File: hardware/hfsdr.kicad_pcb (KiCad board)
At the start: 2 copper layers, 50 x 25 mm, 8 parts, among them J1 USB_C_Receptacle_USB2.0_16P, U1 SN74CBT3253, U2 XLV320ADC6120IRTER, U3 CH32V30xFxPx, U4 XC6206PxxxMR, Y1 Si5351A-B-GT

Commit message: Update schematic
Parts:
- added C1: 1uF, Capacitor_SMD:C_0805_2012Metric_Pad1.18x1.45mm_HandSolder, F.Cu at (128.2, 63.2)
- added C10: 1uF, Capacitor_SMD:C_0805_2012Metric_Pad1.18x1.45mm_HandSolder, F.Cu at (162.2, 81.2)
- added C11: 100nF, Capacitor_SMD:C_0805_2012Metric_Pad1.18x1.45mm_HandSolder, F.Cu at (162.2, 84.2)
- added C12: 100nF, Capacitor_SMD:C_0805_2012Metric_Pad1.18x1.45mm_HandSolder, F.Cu at (162.2, 87.2)
- added C13: 1uF, Capacitor_SMD:C_0805_2012Metric_Pad1.18x1.45mm_HandSolder, F.Cu at (162.2, 90.2)
- added C14: 1uF, Capacitor_SMD:C_0805_2012Metric_Pad1.18x1.45mm_HandSolder, F.Cu at (167.0, 75.2)
- added C15: 1uF, Capacitor_SMD:C_0805_2012Metric_Pad1.18x1.45mm_HandSolder, F.Cu at (167.0, 78.2)
- added C16: 1uF, Capacitor_SMD:C_0805_2012Metric_Pad1.18x1.45mm_HandSolder, F.Cu at (167.0, 81.2)
- added C17: 100nF, Capacitor_SMD:C_0603_1608Metric_Pad1.08x0.95mm_HandSolder, F.Cu at (110.5, 68.2)
- added C18: 100nF, Capacitor_SMD:C_0603_1608Metric_Pad1.08x0.95mm_HandSolder, F.Cu at (110.5, 70.7)
- added C19: 100nF, Capacitor_SMD:C_0805_2012Metric_Pad1.18x1.45mm_HandSolder, F.Cu at (159.1, 42.2)
- added C2: 100nF, Capacitor_SMD:C_0603_1608Metric_Pad1.08x0.95mm_HandSolder, F.Cu at (130.8, 53.8)
- added C20: 100nF, Capacitor_SMD:C_0805_2012Metric_Pad1.18x1.45mm_HandSolder, F.Cu at (159.1, 45.2)
- added C3: 1nF, Capacitor_SMD:C_0805_2012Metric_Pad1.18x1.45mm_HandSolder, F.Cu at (128.2, 55.8)
- added C4: 100nF, Capacitor_SMD:C_0805_2012Metric_Pad1.18x1.45mm_HandSolder, F.Cu at (157.4, 81.2)
- added C5: 100nF, Capacitor_SMD:C_0805_2012Metric_Pad1.18x1.45mm_HandSolder, F.Cu at (157.4, 84.2)
- added C6: 100nF, Capacitor_SMD:C_0805_2012Metric_Pad1.18x1.45mm_HandSolder, F.Cu at (157.4, 87.2)
- added C7: 100nF, Capacitor_SMD:C_0805_2012Metric_Pad1.18x1.45mm_HandSolder, F.Cu at (157.4, 90.2)
- added C8: 100nF, Capacitor_SMD:C_0805_2012Metric_Pad1.18x1.45mm_HandSolder, F.Cu at (162.2, 75.2)
- added C9: 1uF, Capacitor_SMD:C_0805_2012Metric_Pad1.18x1.45mm_HandSolder, F.Cu at (162.2, 78.2)
- added FB1: GZ2012D601TF, Inductor_SMD:L_0201_0603Metric_Pad0.64x0.40mm_HandSolder, F.Cu at (114.7, 81.5)
- added FB2: GZ2012D601TF, Inductor_SMD:L_0201_0603Metric_Pad0.64x0.40mm_HandSolder, F.Cu at (100.6, 79.0)
- added R3: 10k, Resistor_SMD:R_0603_1608Metric_Pad0.98x0.95mm_HandSolder, F.Cu at (118.5, 50.5)
- added R4: 10k, Resistor_SMD:R_0603_1608Metric_Pad0.98x0.95mm_HandSolder, F.Cu at (112.2, 49.4)
- added SW1: RST, Button_Switch_SMD:SW_Push_1P1T_XKB_TS-1187A, F.Cu at (112.2, 44.1)
- added SW2: BOOT0, Button_Switch_SMD:SW_Push_1P1T_XKB_TS-1187A, F.Cu at (121.0, 44.4)
- added U5: MD57E33QA3, Package_TO_SOT_SMD:SOT-23, F.Cu at (127.8, 84.2)
- U3: value CH32V30xFxPx -> CH32V30xRxTx; footprint Package_SO:TSSOP-20_4.4x6.5mm_P0.65mm -> Package_QFP:LQFP-64_10x10mm_P0.5mm
- U4: value XC6206PxxxMR -> MD57E33QA3; footprint Package_TO_SOT_SMD:SOT-23-3 -> Package_TO_SOT_SMD:SOT-23
- moved U1 27.0 mm to (122.4, 76.2), turned to 0 degrees
- moved Y1 24.3 mm to (102.9, 75.9), turned to 0 degrees
- moved U2 15.8 mm to (109.6, 76.0), turned to 0 degrees
- moved U4 14.3 mm to (126.2, 52.8), turned to 180 degrees
- moved U3 11.2 mm to (110.3, 60.5), turned to -90 degrees
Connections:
- J1 pad A4: Net-(J1-VBUS-PadA4) -> +5V
- J1 pad A6: Net-(U3-PB7) -> DP
- J1 pad A7: Net-(U3-PB6) -> DM
- J1 pad A9: Net-(J1-VBUS-PadA4) -> +5V
- J1 pad B4: Net-(J1-VBUS-PadA4) -> +5V
- J1 pad B6: Net-(U3-PB7) -> DP
- J1 pad B7: Net-(U3-PB6) -> DM
- J1 pad B9: Net-(J1-VBUS-PadA4) -> +5V
- R1 pad 1: GND -> Net-(J1-CC2)
- R1 pad 2: Net-(J1-CC2) -> GND
- U3 pad 1: unconnected-(U3-~{RST}-Pad1) -> +3.3V
- U3 pad 12: unconnected-(U3-PA8/PC9-Pad12) -> GND
- U3 pad 13: unconnected-(U3-SWDIO-Pad13) -> Net-(U3-VDDA)
- U3 pad 16: Net-(U3-PB6) -> unconnected-(U3-PA2-Pad16)
- U3 pad 17: Net-(U3-PB7) -> unconnected-(U3-PA3-Pad17)
- U3 pad 19: MCU_XI -> +3.3V
- U3 pad 3: SCL -> unconnected-(U3-PC14-Pad3)
- U3 pad 4: SDA -> unconnected-(U3-PC15-Pad4)
- U3 pad 5: WS -> Net-(U3-OSC_IN)
- U3 pad 6: CK -> unconnected-(U3-OSC_OUT-Pad6)
- U3 pad 7: unconnected-(U3-PB14-Pad7) -> Net-(U3-~{RST})
- U3 pad 8: SD -> unconnected-(U3-PC0-Pad8)
- U3 pad 9: MCK -> unconnected-(U3-PC1-Pad9)
- U4 pad 2: unconnected-(U4-VO-Pad2) -> +5V
- U4 pad 3: unconnected-(U4-VI-Pad3) -> +3.3V
- Y1 pad 1: unconnected-(Y1-VDD-Pad1) -> Net-(Y1-VDD)
- Y1 pad 7: unconnected-(Y1-VDDO-Pad7) -> Net-(Y1-VDDO)
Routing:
- net DP: track 0.00 -> 18.5 mm
- net DM: track 0.00 -> 18.3 mm
- net MCU_XI: track 13.4 -> 0.00 mm
- net +5V: track 0.00 -> 12.2 mm
- net unconnected-(U1-2A-Pad9): track 10.5 -> 0.00 mm
- net Net-(U3-PB7): track 9.99 -> 0.00 mm
- net Net-(U3-PB6): track 9.72 -> 0.00 mm
- net Net-(U1-S0): track 9.67 -> 0.00 mm
- net Net-(U1-2B3): track 9.24 -> 0.00 mm, vias 2 -> 0
- net Net-(U1-S1): track 9.07 -> 0.00 mm
- net MCK: track 8.92 -> 0.00 mm, vias 2 -> 0
- net Net-(U1-2B1): track 8.76 -> 0.00 mm, vias 2 -> 0
- net Net-(U1-2B2): track 8.71 -> 0.00 mm
- net SCL: track 7.48 -> 0.00 mm
- net SD: track 7.16 -> 0.00 mm
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
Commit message: amp and audio
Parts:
- added C21: 100nF, Capacitor_SMD:C_0805_2012Metric_Pad1.18x1.45mm_HandSolder, F.Cu at (149.5, 57.1)
- added C22: 100nF, Capacitor_SMD:C_0805_2012Metric_Pad1.18x1.45mm_HandSolder, F.Cu at (149.5, 60.1)
- added C23: 100nF, Capacitor_SMD:C_0805_2012Metric_Pad1.18x1.45mm_HandSolder, F.Cu at (146.2, 72.8)
- added FB3: GZ2012D601TF, Inductor_SMD:L_0805_2012Metric_Pad1.05x1.20mm_HandSolder, F.Cu at (149.6, 54.2)
- added U6: BGA2817, Package_TO_SOT_SMD:SOT-363_SC-70-6, F.Cu at (154.1, 57.6)
- added U7: TP4054, Package_TO_SOT_SMD:TSOT-23-5, F.Cu at (146.4, 69.0)
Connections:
- C1 pad 1: +5V -> VBUS
- C2 pad 1: +5V -> VBUS
- C3 pad 1: +5V -> VBUS
- J1 pad A4: +5V -> VBUS
- J1 pad A9: +5V -> VBUS
- J1 pad B4: +5V -> VBUS
- J1 pad B9: +5V -> VBUS
- U1 pad 9: unconnected-(U1-2A-Pad9) -> Net-(U1-2A)
- U3 pad 20: unconnected-(U3-PA4-Pad20) -> DAC1_OUT
- U3 pad 21: unconnected-(U3-PA5-Pad21) -> DAC2_OUT
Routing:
- net +5V: track 12.2 -> 9.52 mm
- net VBUS: track 0.00 -> 2.68 mm

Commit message: arrange pcb
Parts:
- added C24: 100nF, Capacitor_SMD:C_0805_2012Metric_Pad1.18x1.45mm_HandSolder, F.Cu at (102.5, 49.5)
- added C25: 1uF, Capacitor_SMD:C_0805_2012Metric_Pad1.18x1.45mm_HandSolder, F.Cu at (109.0, 49.5)
- added C26: 100nF, Capacitor_SMD:C_0805_2012Metric_Pad1.18x1.45mm_HandSolder, F.Cu at (101.0, 51.0)
- added C27: 1uF, Capacitor_SMD:C_0805_2012Metric_Pad1.18x1.45mm_HandSolder, F.Cu at (159.8, 69.8)
- added FB4: GZ2012D601TF, Inductor_SMD:L_0805_2012Metric_Pad1.05x1.20mm_HandSolder, F.Cu at (164.7, 60.6)
- added FB5: GZ2012D601TF, Inductor_SMD:L_0805_2012Metric_Pad1.05x1.20mm_HandSolder, F.Cu at (164.7, 63.4)
- added FB6: GZ2012D601TF, Inductor_SMD:L_0805_2012Metric_Pad1.05x1.20mm_HandSolder, F.Cu at (164.7, 66.1)
- added FB7: GZ2012D601TF, Inductor_SMD:L_0805_2012Metric_Pad1.05x1.20mm_HandSolder, F.Cu at (164.7, 68.9)
- added R5: 10k, Resistor_SMD:R_0603_1608Metric_Pad0.98x0.95mm_HandSolder, F.Cu at (99.0, 47.5)
- added R6: 10k, Resistor_SMD:R_0603_1608Metric_Pad0.98x0.95mm_HandSolder, F.Cu at (100.8, 46.0)
- added U8: NS4263_C2829094, easyeda:SOIC-16_L9.9-W3.9-P1.27-LS6.0-BL, F.Cu at (99.5, 38.6)
- FB1, FB2: footprint Inductor_SMD:L_0201_0603Metric_Pad0.64x0.40mm_HandSolder -> Inductor_SMD:L_0805_2012Metric_Pad1.05x1.20mm_HandSolder
- moved U5 48.5 mm to (93.8, 49.8), turned to -90 degrees
- moved U1 36.4 mm to (88.5, 63.0)
- moved C17 34.6 mm to (141.9, 82.8)
- moved FB1 28.3 mm to (115.9, 53.2), turned to 180 degrees
- moved FB2 27.6 mm to (92.2, 52.8), turned to -90 degrees
- moved C18 26.7 mm to (134.4, 82.8)
- moved Y1 21.4 mm to (95.0, 56.0), turned to 90 degrees
- moved U2 19.5 mm to (95.8, 62.2), turned to 90 degrees
- moved SW1 11.4 mm to (123.5, 42.5)
- moved SW2 11.4 mm to (132.2, 42.8)
- moved U3 2.37 mm to (108.1, 59.6), turned to -135 degrees
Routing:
- net DP: track 18.5 -> 3.75 mm
- net DM: track 18.3 -> 4.76 mm
- net SCL: track 0.00 -> 11.2 mm
- net MCK: track 0.00 -> 10.2 mm
- net SDA: track 0.00 -> 9.74 mm
- net +3.3V: track 0.00 -> 5.90 mm
- net SD: track 0.00 -> 5.70 mm
- net CK: track 0.00 -> 5.07 mm
- net WS: track 0.00 -> 4.66 mm
- net Net-(U3-VDDA): track 0.00 -> 4.49 mm

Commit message: battery switching
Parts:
- added C28: 1uF, Capacitor_SMD:C_0805_2012Metric_Pad1.18x1.45mm_HandSolder, F.Cu at (123.2, 50.5)
- added D1: 1N5819WS, Diode_SMD:D_SOD-323, F.Cu at (127.0, 53.5)
- added Q1: AO3401A, Package_TO_SOT_SMD:SOT-23, F.Cu at (123.5, 53.4)
- added R7: 100k, Resistor_SMD:R_0805_2012Metric_Pad1.20x1.40mm_HandSolder, F.Cu at (124.0, 56.5)
- added R8: 2k, Resistor_SMD:R_0805_2012Metric_Pad1.20x1.40mm_HandSolder, F.Cu at (150.8, 70.3)
- added R9: 2k, Resistor_SMD:R_0805_2012Metric_Pad1.20x1.40mm_HandSolder, F.Cu at (150.8, 73.2)
- C17, C18, C2: footprint Capacitor_SMD:C_0603_1608Metric_Pad1.08x0.95mm_HandSolder -> Capacitor_SMD:C_0805_2012Metric_Pad1.18x1.45mm_HandSolder
- R1, R2, R3, R4, R5, R6: footprint Resistor_SMD:R_0603_1608Metric_Pad0.98x0.95mm_HandSolder -> Resistor_SMD:R_0805_2012Metric_Pad1.20x1.40mm_HandSolder
- U1: footprint Package_SO:TSSOP-16_4.4x5mm_P0.65mm -> Package_SO:SOIC-16_3.9x9.9mm_P1.27mm
- moved C13 55.0 mm to (120.5, 54.3), turned to -90 degrees
- moved U7 29.8 mm to (126.4, 47.0)
- moved U6 16.3 mm to (146.2, 43.2)
- moved U4 7.35 mm to (119.2, 50.5)
- moved R3 2.26 mm to (116.2, 50.2)
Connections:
- U7 pad 1: unconnected-(U7-~{CHRG}-Pad1) -> Net-(D2-K)
- U7 pad 5: unconnected-(U7-PROG-Pad5) -> Net-(U7-PROG)
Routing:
- net VBUS: track 2.68 -> 12.7 mm
- net GND: track 8.65 -> 6.61 mm
- net +5V: track 9.52 -> 7.84 mm

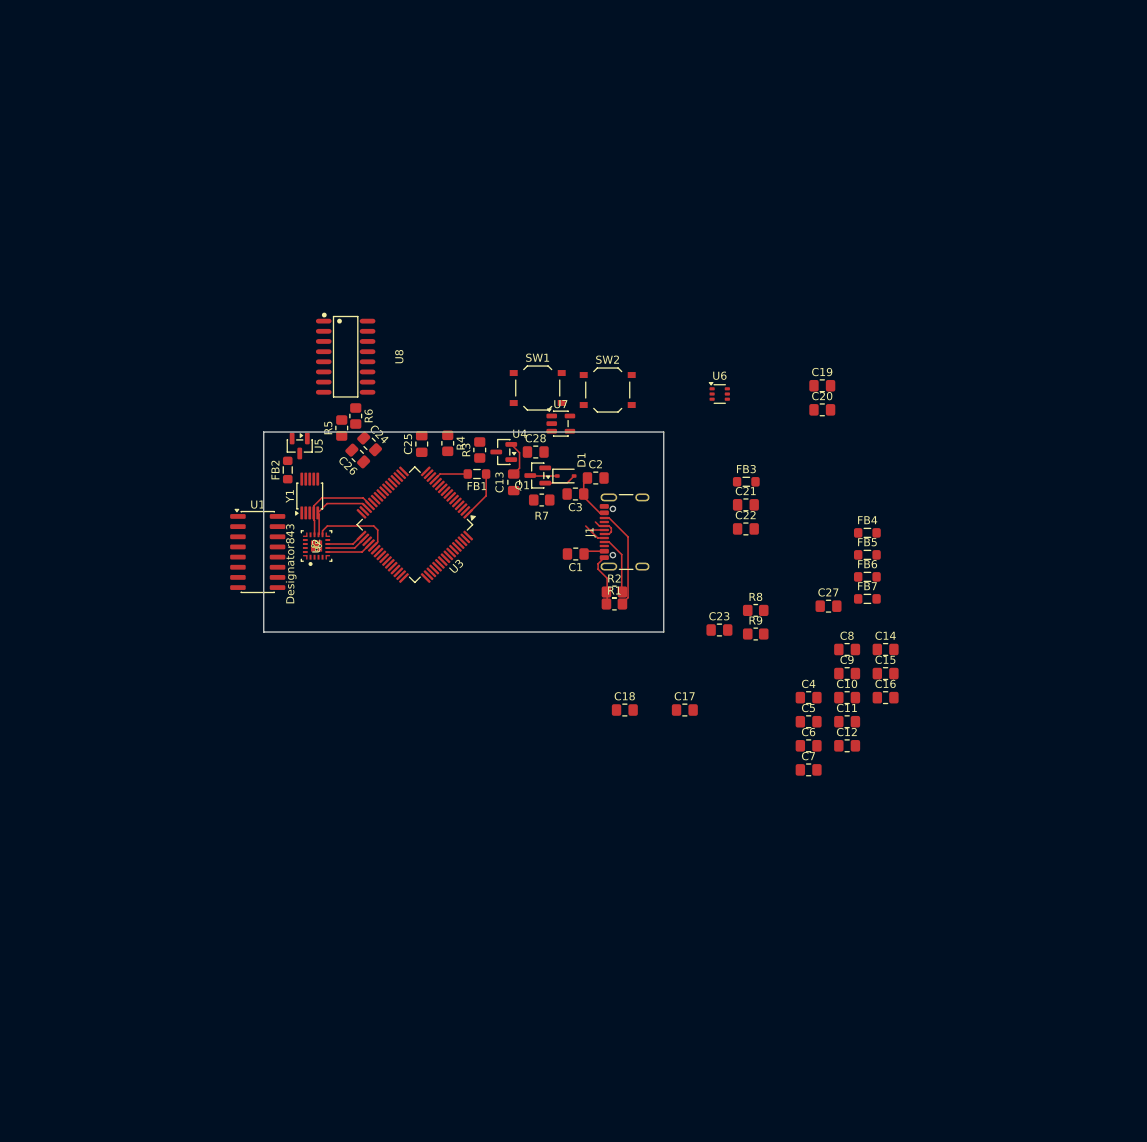
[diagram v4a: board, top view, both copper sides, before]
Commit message: initial component layout
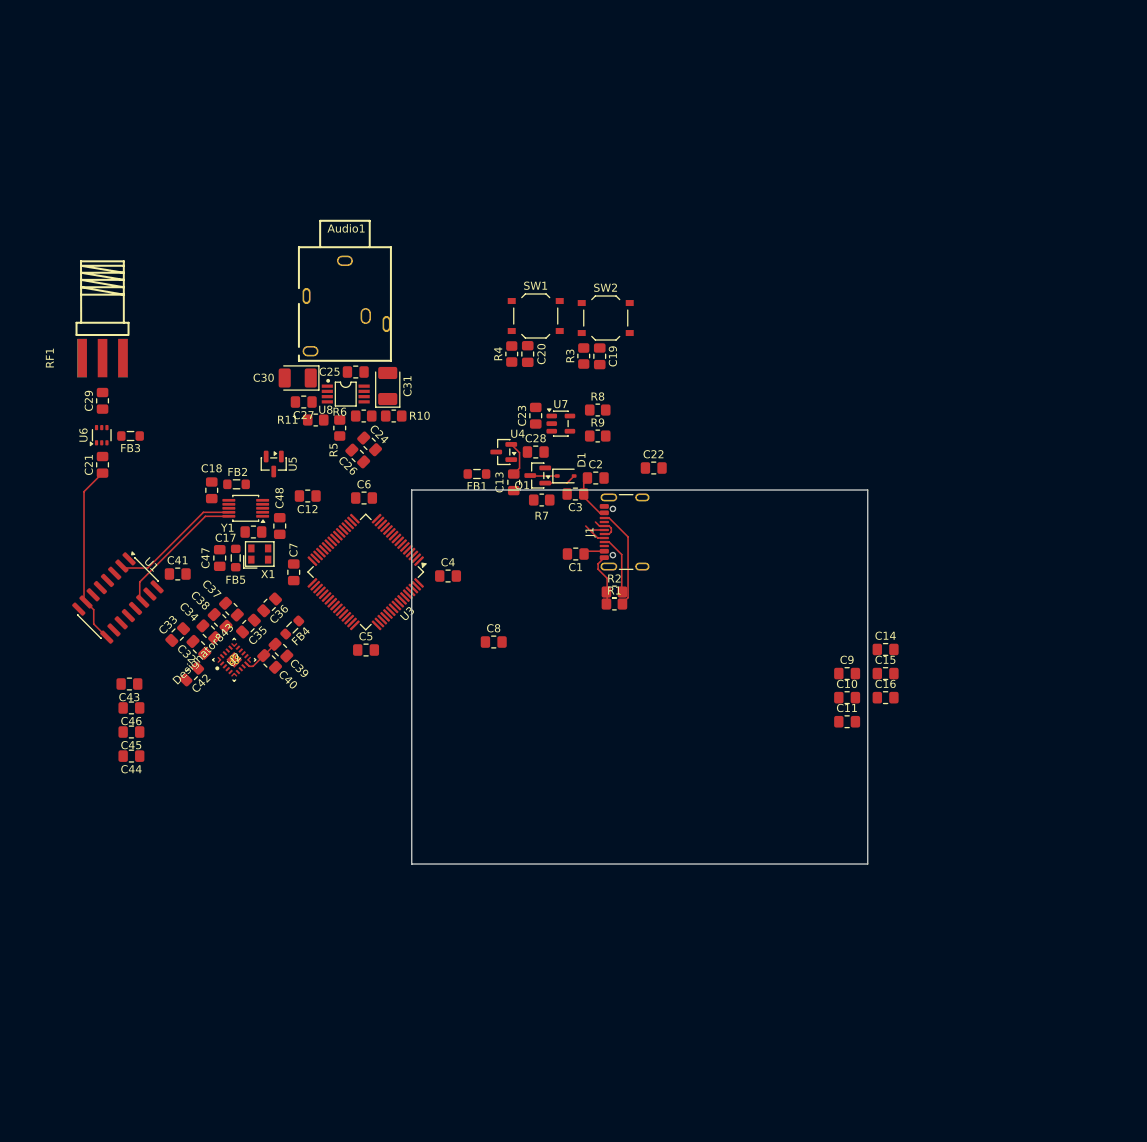
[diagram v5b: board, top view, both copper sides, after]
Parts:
- removed FB6, FB7: GZ2012D601TF, Inductor_SMD:L_0805_2012Metric_Pad1.05x1.20mm_HandSolder
- added Audio1: PJ-3240-5A, easyeda:AUDIO-TH_PJ-3240-5A, F.Cu at (99.6, 32.2)
- added C29: 1uF, Capacitor_SMD:C_0805_2012Metric_Pad1.18x1.45mm_HandSolder, F.Cu at (69.1, 44.1)
- added C30: 100uF, Capacitor_Tantalum_SMD:CP_EIA-3528-15_AVX-H_HandSolder, F.Cu at (93.5, 41.2)
- added C31: 100uF, Capacitor_Tantalum_SMD:CP_EIA-3528-15_AVX-H_HandSolder, F.Cu at (104.8, 42.2)
- added C32: 1uF, Capacitor_SMD:C_0805_2012Metric_Pad1.18x1.45mm_HandSolder, F.Cu at (81.1, 74.9)
- added C33: 10uF, Capacitor_SMD:C_0805_2012Metric_Pad1.18x1.45mm_HandSolder, F.Cu at (78.5, 73.3)
- added C34: 100nF, Capacitor_SMD:C_0805_2012Metric_Pad1.18x1.45mm_HandSolder, F.Cu at (82.4, 73.0)
- added C35: 100nF, Capacitor_SMD:C_0805_2012Metric_Pad1.18x1.45mm_HandSolder, F.Cu at (87.3, 72.3)
- added C36: 10uF, Capacitor_SMD:C_0805_2012Metric_Pad1.18x1.45mm_HandSolder, F.Cu at (90.0, 69.6)
- added C37: 100nF, Capacitor_SMD:C_0805_2012Metric_Pad1.18x1.45mm_HandSolder, F.Cu at (85.2, 70.1)
- added C38: 1uF, Capacitor_SMD:C_0805_2012Metric_Pad1.18x1.45mm_HandSolder, F.Cu at (83.8, 71.6)
- added C39: 100nF, Capacitor_SMD:C_0805_2012Metric_Pad1.18x1.45mm_HandSolder, F.Cu at (91.4, 75.3)
- added C40: 10uF, Capacitor_SMD:C_0805_2012Metric_Pad1.18x1.45mm_HandSolder, F.Cu at (90.0, 76.7)
- added C41: 100nF, Capacitor_SMD:C_0805_2012Metric_Pad1.18x1.45mm_HandSolder, F.Cu at (78.5, 65.8)
- added C42: 1uF, Capacitor_SMD:C_0805_2012Metric_Pad1.18x1.45mm_HandSolder, F.Cu at (80.2, 78.2)
- added C43: 2.2nF, Capacitor_SMD:C_0805_2012Metric_Pad1.18x1.45mm_HandSolder, F.Cu at (72.5, 79.5)
- added C44: 2.2nF, Capacitor_SMD:C_0805_2012Metric_Pad1.18x1.45mm_HandSolder, F.Cu at (72.7, 88.5)
- added C45: 2.2nF, Capacitor_SMD:C_0805_2012Metric_Pad1.18x1.45mm_HandSolder, F.Cu at (72.7, 85.5)
- added C46: 2.2nF, Capacitor_SMD:C_0805_2012Metric_Pad1.18x1.45mm_HandSolder, F.Cu at (72.7, 82.5)
- added C47: 100nF, Capacitor_SMD:C_0805_2012Metric_Pad1.18x1.45mm_HandSolder, F.Cu at (83.8, 63.8)
- added C48: 100nF, Capacitor_SMD:C_0805_2012Metric_Pad1.18x1.45mm_HandSolder, F.Cu at (91.2, 59.8)
- added R10: 20k, Resistor_SMD:R_0805_2012Metric_Pad1.20x1.40mm_HandSolder, F.Cu at (105.5, 46.0)
- added R11: 20k, Resistor_SMD:R_0805_2012Metric_Pad1.20x1.40mm_HandSolder, F.Cu at (95.8, 46.5)
- added RF1: BWSMA-KE-P001, easyeda:SMA-SMD_BWSMA-KE-P001, F.Cu at (69.1, 38.8)
- added X1: 2T024000VX, easyeda:OSC-SMD_4P-L2.5-W2.0-BL_X1G0054210307, F.Cu at (88.8, 63.2)
- C21: value 100nF -> 1uF
- C24, C26: value 100nF -> 470nF
- C3: value 1nF -> 2.2nF
- R5, R6: value 10k -> 20k
- U8: value NS4263_C2829094 -> LM4809; footprint easyeda:SOIC-16_L9.9-W3.9-P1.27-LS6.0-BL -> easyeda:MSOP-8_L3.0-W3.0-P0.65-LS4.9-BL
- moved C21 80.6 mm to (69.1, 52.1), turned to 90 degrees
- moved FB5 79.0 mm to (85.8, 63.8), turned to 90 degrees
- moved U6 77.4 mm to (69.0, 48.4), turned to 90 degrees
- moved FB3 77.2 mm to (72.6, 48.5), turned to 180 degrees
- moved C12 74.3 mm to (94.8, 56.0), turned to 180 degrees
- moved FB4 72.9 mm to (92.8, 72.4), turned to -135 degrees
- moved C27 70.4 mm to (94.2, 44.2), turned to 180 degrees
- moved C7 68.9 mm to (93.0, 65.5), turned to -90 degrees
- moved C6 63.6 mm to (101.8, 56.2)
- moved C18 58.5 mm to (82.8, 55.3), turned to 90 degrees
- moved C17 58.3 mm to (88.0, 60.5)
- moved C5 56.0 mm to (102.0, 75.2)
- moved C4 47.6 mm to (112.3, 66.0)
- moved C8 44.2 mm to (118.0, 74.2)
- moved C20 37.5 mm to (122.2, 38.2), turned to 90 degrees
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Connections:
- C21 pad 1: Net-(U1-2A) -> Net-(U1-1A)
- C27 pad 1: Net-(U8-VREF) -> Net-(U8-BYP)
- FB4 pad 1: unconnected-(FB4-Pad1) -> +3.3V
- FB4 pad 2: Net-(U8-VOLN) -> Net-(U1-VCC)
- FB5 pad 1: unconnected-(FB5-Pad1) -> +3.3VA
- FB5 pad 2: Net-(U8-VOLP) -> Net-(X1-VDD)
- R5 pad 2: Net-(U8-INRN) -> Net-(U8-IN1)
- U1 pad 1: unconnected-(U1-1~{OE}-Pad1) -> GND
- U1 pad 15: unconnected-(U1-2~{OE}-Pad15) -> GND
- U1 pad 16: unconnected-(U1-VCC-Pad16) -> Net-(U1-VCC)
- U1 pad 7: unconnected-(U1-1A-Pad7) -> Net-(U1-1A)
- U1 pad 9: Net-(U1-2A) -> Net-(U1-1A)
- U2 pad 14: unconnected-(U2-DREG-Pad14) -> Net-(U2-DREG)
- U2 pad 16: unconnected-(U2-AVDD-Pad16) -> +3.3VA
- U2 pad 17: unconnected-(U2-AREG-Pad17) -> Net-(U2-AREG)
- U2 pad 18: unconnected-(U2-VREF-Pad18) -> Net-(U2-VREF)
- U2 pad 19: unconnected-(U2-MICBIAS_GPI2-Pad19) -> Net-(U2-MICBIAS_GPI2)
- U2 pad 9: unconnected-(U2-IOVDD-Pad9) -> Net-(U1-VCC)
- U6 pad 6: unconnected-(U6-Pad6) -> Net-(C29-Pad1)
- U8 pad 1: unconnected-(U8-SD-Pad1) -> Net-(U8-V01)
- U8 pad 2: GND -> Net-(U8-IN1)
- U8 pad 3: Net-(U8-VOLP) -> Net-(U8-BYP)
- U8 pad 4: +3.3V -> GND
- U8 pad 5: Net-(U8-VOLN) -> unconnected-(U8-~{SD}-Pad5)
- U8 pad 7: GND -> Net-(U8-V02)
- U8 pad 8: unconnected-(U8-NC-Pad8) -> +3.3V
- Y1 pad 2: unconnected-(Y1-XA-Pad2) -> Net-(Y1-XA)
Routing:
- net Net-(U1-1A): track 0.00 -> 22.6 mm
- net Net-(U1-S0): track 0.00 -> 17.1 mm
- net Net-(U1-S1): track 0.00 -> 16.4 mm
- net SCL: track 11.2 -> 0.00 mm
- net MCK: track 10.2 -> 0.00 mm
- net SDA: track 9.74 -> 0.00 mm
- net +3.3V: track 5.90 -> 0.00 mm
- net SD: track 5.70 -> 0.00 mm
- net CK: track 5.07 -> 0.00 mm
- net Net-(U1-VCC): track 0.00 -> 4.87 mm
- net WS: track 4.66 -> 0.00 mm
- net Net-(U3-VDDA): track 4.49 -> 0.00 mm
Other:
- board size 50 x 25 mm -> 57 x 46.8 mm

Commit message: initial screen
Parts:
- added FPC1: FPC-05F-18PH20, easyeda:FPC-SMD_18P-P0.50_FPC-05F-18PH20, F.Cu at (101.8, 85.2)
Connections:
- U3 pad 55: unconnected-(U3-PB3-Pad55) -> SCL_SCK
- U3 pad 57: unconnected-(U3-PB5-Pad57) -> SDA_MOSI

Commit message: feat: add rough art
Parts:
- removed Audio1: PJ-3240-5A, easyeda:AUDIO-TH_PJ-3240-5A
- added G***: LOGO, LOGO, F.Cu at (117.6, 67.4)
- moved SW1 64.8 mm to (128.0, 98.1)
- moved SW2 64.6 mm to (138.0, 98.1)
- moved C10 9.39 mm to (152.8, 81.2)
- moved C11 9.39 mm to (152.8, 84.2)
- moved C9 9.39 mm to (152.8, 78.2)
- moved C14 9.39 mm to (157.6, 75.2)
- moved C15 9.39 mm to (157.6, 78.2)
- moved C16 9.39 mm to (157.6, 81.2)
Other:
- board size 57 x 46.8 mm -> 100 x 99.4 mm
